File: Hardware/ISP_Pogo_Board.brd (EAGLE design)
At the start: 17.8 x 50.8 mm, 12 parts, among them J2 AVR_SPI_PRG_6NS

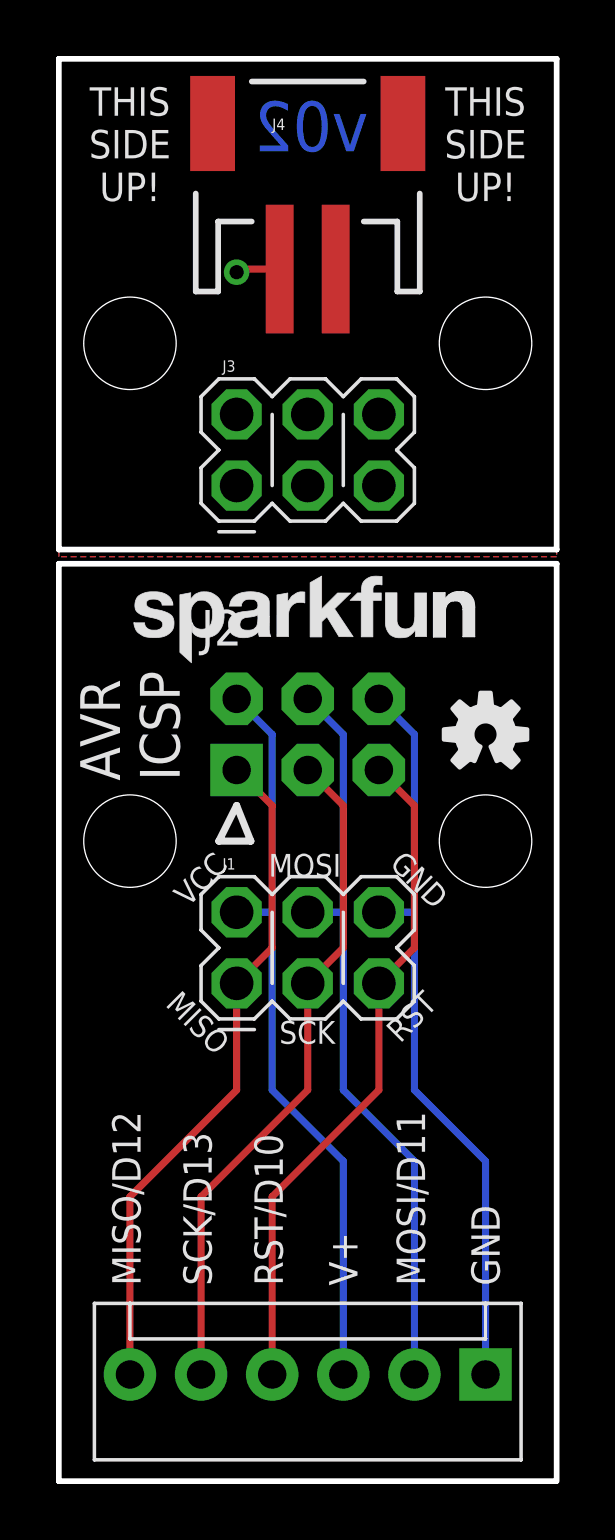
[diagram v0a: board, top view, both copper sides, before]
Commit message: Changed for v10: Made planes not overlap vscore region Increased annular ring on pogo pin pads
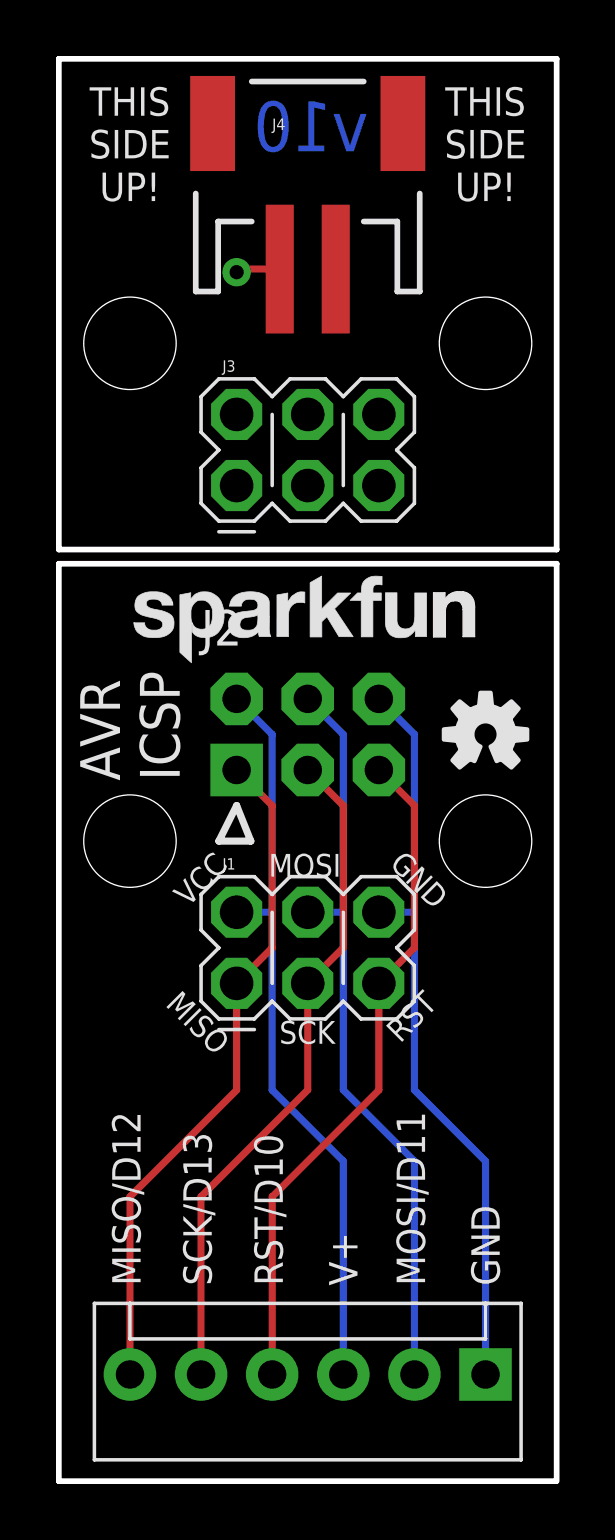
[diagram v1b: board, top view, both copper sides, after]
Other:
- board text added: "v10"
- board text removed: "v02"
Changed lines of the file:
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@@
 <layer number="23" name="tOrigins" color="15" fill="1" visible="yes" active="yes"/>
 <layer number="24" name="bOrigins" color="15" fill="1" visible="yes" active="yes"/>
-<layer number="25" name="tNames" color="7" fill="1" visible="yes" active="yes"/>
+<layer number="25" name="tNames" color="7" fill="1" visible="no" active="yes"/>
 <layer number="26" name="bNames" color="7" fill="1" visible="no" active="yes"/>
 <layer number="27" name="tValues" color="7" fill="1" visible="no" active="yes"/>
@@
 <text x="4.318" y="25.019" size="1.4224" layer="21" font="vector" ratio="15" rot="R90">AVR
 ICSP</text>
-<text x="11.049" y="47.498" size="1.778" layer="16" font="vector" ratio="15" rot="MR0">v02</text>
+<text x="11.049" y="47.498" size="1.778" layer="16" font="vector" ratio="15" rot="MR0">v10</text>
 <wire x1="0" y1="33.274" x2="17.78" y2="33.274" width="0.2032" layer="20"/>
 <wire x1="17.78" y1="32.766" x2="0" y2="32.766" width="0.2032" layer="20"/>
@@
 </class>
 </classes>
-<designrules name="default">
-<description language="de">&lt;b&gt;EAGLE Design Rules&lt;/b&gt;
-&lt;p&gt;
-Die Standard-Design-Rules sind so gewählt, dass sie für
-die meisten Anwendungen passen. Sollte ihre Platine
-besondere Anforderungen haben, treffen Sie die erforderlichen
-Einstellungen hier und speichern die Design Rules unter
-einem neuen Namen ab.</description>
+<designrules name="Sparkfun">
 <description language="en">&lt;b&gt;EAGLE Design Rules&lt;/b&gt;
 &lt;p&gt;
@@
 <param name="mdViaViaSameLayer" value="8mil"/>
 <param name="mnLayersViaInSmd" value="2"/>
-<param name="mdCopperDimension" value="40mil"/>
+<param name="mdCopperDimension" value="8mil"/>
 <param name="mdDrill" value="8mil"/>
 <param name="mdSmdStop" value="0mil"/>
-<param name="msWidth" value="10mil"/>
-<param name="msDrill" value="24mil"/>
+<param name="msWidth" value="8mil"/>
+<param name="msDrill" value="20mil"/>
 <param name="msMicroVia" value="9.99mm"/>
 <param name="msBlindViaRatio" value="0.5"/>
@@
 <param name="rvMicroViaOuter" value="0.25"/>
 <param name="rvMicroViaInner" value="0.25"/>
-<param name="rlMinPadTop" value="10mil"/>
+<param name="rlMinPadTop" value="12mil"/>
 <param name="rlMaxPadTop" value="20mil"/>
 <param name="rlMinPadInner" value="10mil"/>
 <param name="rlMaxPadInner" value="20mil"/>
-<param name="rlMinPadBottom" value="10mil"/>
+<param name="rlMinPadBottom" value="12mil"/>
 <param name="rlMaxPadBottom" value="20mil"/>
-<param name="rlMinViaOuter" value="8mil"/>
+<param name="rlMinViaOuter" value="10mil"/>
 <param name="rlMaxViaOuter" value="20mil"/>
-<param name="rlMinViaInner" value="8mil"/>
+<param name="rlMinViaInner" value="10mil"/>
 <param name="rlMaxViaInner" value="20mil"/>
 <param name="rlMinMicroViaOuter" value="4mil"/>
@@
 <param name="mlMinCreamFrame" value="0mil"/>
 <param name="mlMaxCreamFrame" value="0mil"/>
-<param name="mlViaStopLimit" value="0mil"/>
+<param name="mlViaStopLimit" value="20mil"/>
 <param name="srRoundness" value="0"/>
 <param name="srMinRoundness" value="0mil"/>
@@
 <vertex x="0" y="50.8"/>
 <vertex x="17.78" y="50.8"/>
-<vertex x="17.78" y="33.02"/>
-<vertex x="0" y="33.02"/>
+<vertex x="17.78" y="33.274"/>
+<vertex x="0" y="33.274"/>
 </polygon>
 </signal>
@@
 <vertex x="0" y="50.8"/>
 <vertex x="17.78" y="50.8"/>
-<vertex x="17.78" y="33.02"/>
-<vertex x="0" y="33.02"/>
+<vertex x="17.78" y="33.274"/>
+<vertex x="0" y="33.274"/>
 </polygon>
 <wire x1="7.89" y1="43.29" x2="6.46" y2="43.29" width="0.254" layer="1"/>
